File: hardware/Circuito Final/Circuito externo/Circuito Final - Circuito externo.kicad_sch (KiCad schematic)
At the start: 34 parts, among them J1 Conn_02x19_Odd_Even, J2 Conn_02x19_Odd_Even, J3 Conn_01x02, J4 Conn_01x02, SW1 SW_SPDT, SW2 SW_DIP_x04, U1 Opamp_Quad, U2 ICL7660

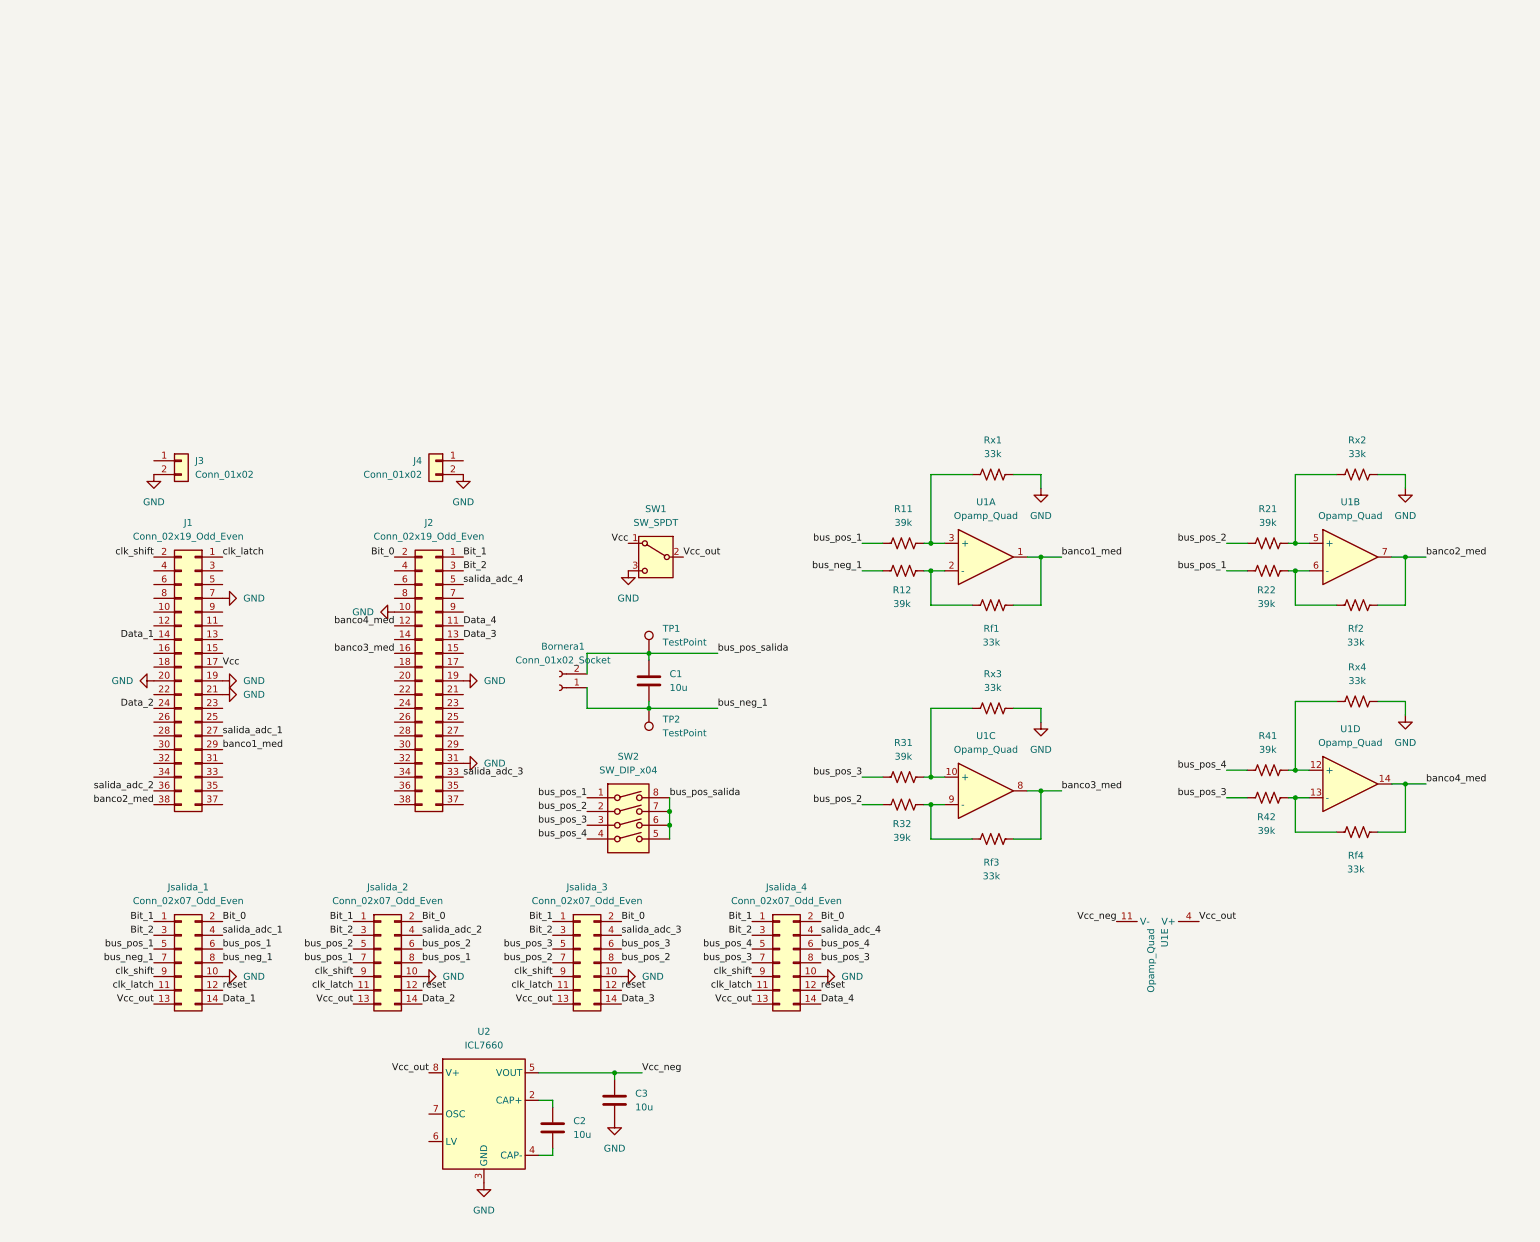
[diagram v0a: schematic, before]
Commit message: sube nuevas conexiones, falta conectar los buses a los conectores
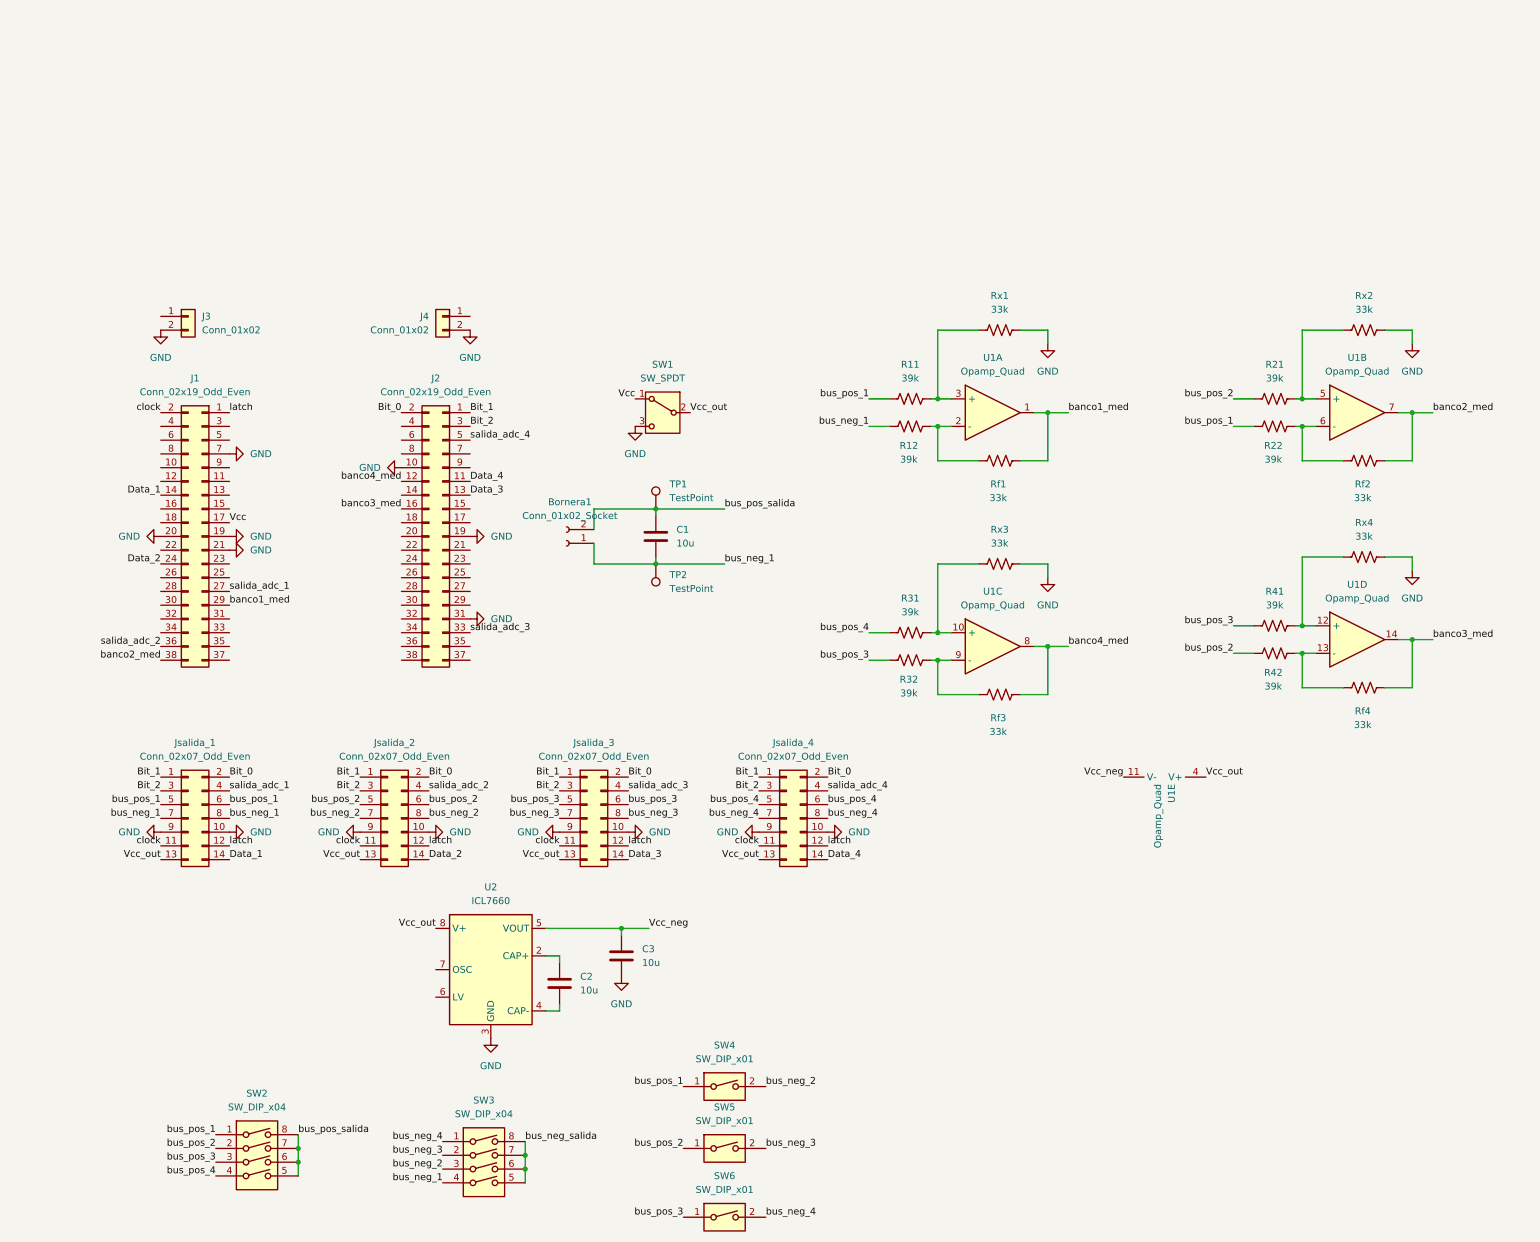
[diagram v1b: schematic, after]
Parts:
- added SW3: SW_DIP_x04, Button_Switch_THT:SW_DIP_SPSTx04_Slide_9.78x12.34mm_W7.62mm_P2.54mm, symbol Switch:SW_DIP_x04
- added SW4, SW5, SW6: SW_DIP_x01, Button_Switch_THT:SW_DIP_SPSTx01_Slide_6.7x4.1mm_W7.62mm_P2.54mm_LowProfile, symbol Switch:SW_DIP_x01
- TP1, TP2: footprint (none) -> TestPoint:TestPoint_Keystone_5005-5009_Compact
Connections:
- net GND: now also Jsalida_1.9 (Pin_9), Jsalida_2.9 (Pin_9), Jsalida_3.9 (Pin_9), Jsalida_4.9 (Pin_9)
- net banco3_med: now also Rf4.2, U1.14; no longer Rf3.2, U1.8
- net banco4_med: now also Rf3.2, U1.8; no longer Rf4.2, U1.14
- net bus_neg_1: now also SW3.4
- net bus_pos_1: now also SW4.1; no longer Jsalida_2.7 (Pin_7), Jsalida_2.8 (Pin_8)
- net bus_pos_2: now also R42.2, SW5.1; no longer Jsalida_3.7 (Pin_7), Jsalida_3.8 (Pin_8), R32.2
- net bus_pos_3: now also R32.2, R41.1, SW6.1; no longer Jsalida_4.7 (Pin_7), Jsalida_4.8 (Pin_8), R31.1, R42.2
- net bus_pos_4: now also R31.1; no longer R41.1
- net clk_latch renamed clock
- net clock: now also J1.2 (Pin_2); no longer J1.1 (Pin_1)
- removed net clk_shift: J1.2 (Pin_2), Jsalida_1.9 (Pin_9), Jsalida_2.9 (Pin_9), Jsalida_3.9 (Pin_9), Jsalida_4.9 (Pin_9)
- net reset renamed latch
- net latch: now also J1.1 (Pin_1)
- new net bus_neg_2: Jsalida_2.7 (Pin_7), Jsalida_2.8 (Pin_8), SW3.3, SW4.2
- new net bus_neg_3: Jsalida_3.7 (Pin_7), Jsalida_3.8 (Pin_8), SW3.2, SW5.2
- new net bus_neg_4: Jsalida_4.7 (Pin_7), Jsalida_4.8 (Pin_8), SW3.1, SW6.2
- new net bus_neg_salida: SW3.5, SW3.6, SW3.7, SW3.8
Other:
- moved on the sheet: Bornera1, C1, C2, C3, J1, J2, J3, J4, Jsalida_1, Jsalida_2, Jsalida_3, Jsalida_4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

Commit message: sube mediciones de switching
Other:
- moved on the sheet: SW1
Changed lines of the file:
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@@
 	(wire
 		(pts
+			(xy 152.4 39.37) (xy 116.84 39.37)
+		)
+		(stroke
+			(width 0)
+			(type default)
+		)
+	)
+	(wire
+		(pts
 			(xy 182.88 30.48) (xy 175.26 30.48)
 		)
@@
 	)
 	(label "Vcc_out"
-		(at 129.54 45.72 0)
+		(at 152.4 39.37 0)
 		(effects
 			(font
@@
 	)
 	(label "Vcc"
-		(at 119.38 43.18 180)
+		(at 106.68 36.83 180)
 		(effects
 			(font
@@
 	(symbol
 		(lib_id "Switch:SW_SPDT")
-		(at 124.46 45.72 0)
+		(at 111.76 39.37 0)
 		(mirror y)
 		(unit 1)
@@
 		(fields_autoplaced yes)
 		(property "Reference" "SW1"
-			(at 124.46 36.83 0)
+			(at 111.76 30.48 0)
 			(show_name no)
 			(do_not_autoplace no)
@@
 		)
 		(property "Value" "SW_SPDT"
-			(at 124.46 39.37 0)
+			(at 111.76 33.02 0)
 			(show_name no)
 			(do_not_autoplace no)
@@
 		)
 		(property "Footprint" "Button_Switch_THT:SW_Slide_SPDT_Straight_CK_OS102011MS2Q"
-			(at 124.46 45.72 0)
+			(at 111.76 39.37 0)
 			(hide yes)
 			(show_name no)
@@
 		)
 		(property "Datasheet" ""
-			(at 124.46 53.34 0)
+			(at 111.76 46.99 0)
 			(hide yes)
 			(show_name no)
@@
 		)
 		(property "Description" "Switch, single pole double throw"
-			(at 124.46 45.72 0)
+			(at 111.76 39.37 0)
 			(hide yes)
 			(show_name no)
@@
 	(symbol
 		(lib_id "power:GND")
-		(at 119.38 48.26 0)
+		(at 106.68 41.91 0)
 		(mirror y)
 		(unit 1)
@@
 		(fields_autoplaced yes)
 		(property "Reference" "#PWR06"
-			(at 119.38 54.61 0)
+			(at 106.68 48.26 0)
 			(hide yes)
 			(show_name no)
@@
 		)
 		(property "Value" "GND"
-			(at 119.38 53.34 0)
+			(at 106.68 46.99 0)
 			(show_name no)
 			(do_not_autoplace no)
@@
 		)
 		(property "Footprint" ""
-			(at 119.38 48.26 0)
+			(at 106.68 41.91 0)
 			(hide yes)
 			(show_name no)
@@
 		)
 		(property "Datasheet" ""
-			(at 119.38 48.26 0)
+			(at 106.68 41.91 0)
 			(hide yes)
 			(show_name no)
@@
 		)
 		(property "Description" "Power symbol creates a global label with name \"GND\" , ground"
-			(at 119.38 48.26 0)
+			(at 106.68 41.91 0)
 			(hide yes)
 			(show_name no)

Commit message: sube mediciones y comienza devuelta el conexionado del pcb
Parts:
- added Q1, Q2: FDMS6681Z, FDMS6681Z, symbol FDMS6681Z:FDMS6681Z
- added Q3: MMBT2222A, Package_TO_SOT_SMD:SOT-23, symbol Transistor_BJT:MMBT2222A
- added R1: R, symbol Device:R
- added U3: INA180A1, Package_TO_SOT_SMD:SOT-23-5, symbol Amplifier_Current:INA180A1
- SW2, SW3: footprint Button_Switch_THT:SW_DIP_SPSTx04_Slide_9.78x12.34mm_W7.62mm_P2.54mm -> Button_Switch_THT:SW_DIP_SPSTx04_Slide_6.7x11.72mm_W7.62mm_P2.54mm_LowProfile
- SW4, SW5, SW6: footprint Button_Switch_THT:SW_DIP_SPSTx01_Slide_6.7x4.1mm_W7.62mm_P2.54mm_LowProfile -> Button_Switch_THT:SW_DIP_SPSTx01_Slide_9.78x4.72mm_W7.62mm_P2.54mm
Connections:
- net GND: now also Q3.2 (E), U3.2 (GND); no longer SW1.3 (C)
- net Vcc: now also Q1.5 (D_1), Q1.6 (D_2), Q1.7 (D_3), Q1.8 (D_4), Q1.9 (D_5); no longer SW1.1 (A)
- net Vcc_out: now also U3.5 (V+)
- net llave_de_emergencia: now reaches J2.23 (Pin_23)
- net llave_de_emergencia: now also R1.2
- new net: Q3.1 (B), R1.1
- new net: Q1.4 (G), Q2.4 (G), Q3.3 (C)
- new net: Q1.1 (S_1), Q1.2 (S_2), Q1.3 (S_3), Q2.1 (S_1), Q2.2 (S_2), Q2.3 (S_3)
- new net: Q2.5 (D_1), Q2.6 (D_2), Q2.7 (D_3), Q2.8 (D_4), Q2.9 (D_5), SW1.1 (A)
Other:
- moved on the sheet: Bornera1, C1, C2, C3, J1, J2, J3, J4, Jsalida_1, Jsalida_2, Jsalida_3, Jsalida_4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
